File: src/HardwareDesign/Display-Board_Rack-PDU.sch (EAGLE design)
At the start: 46 parts

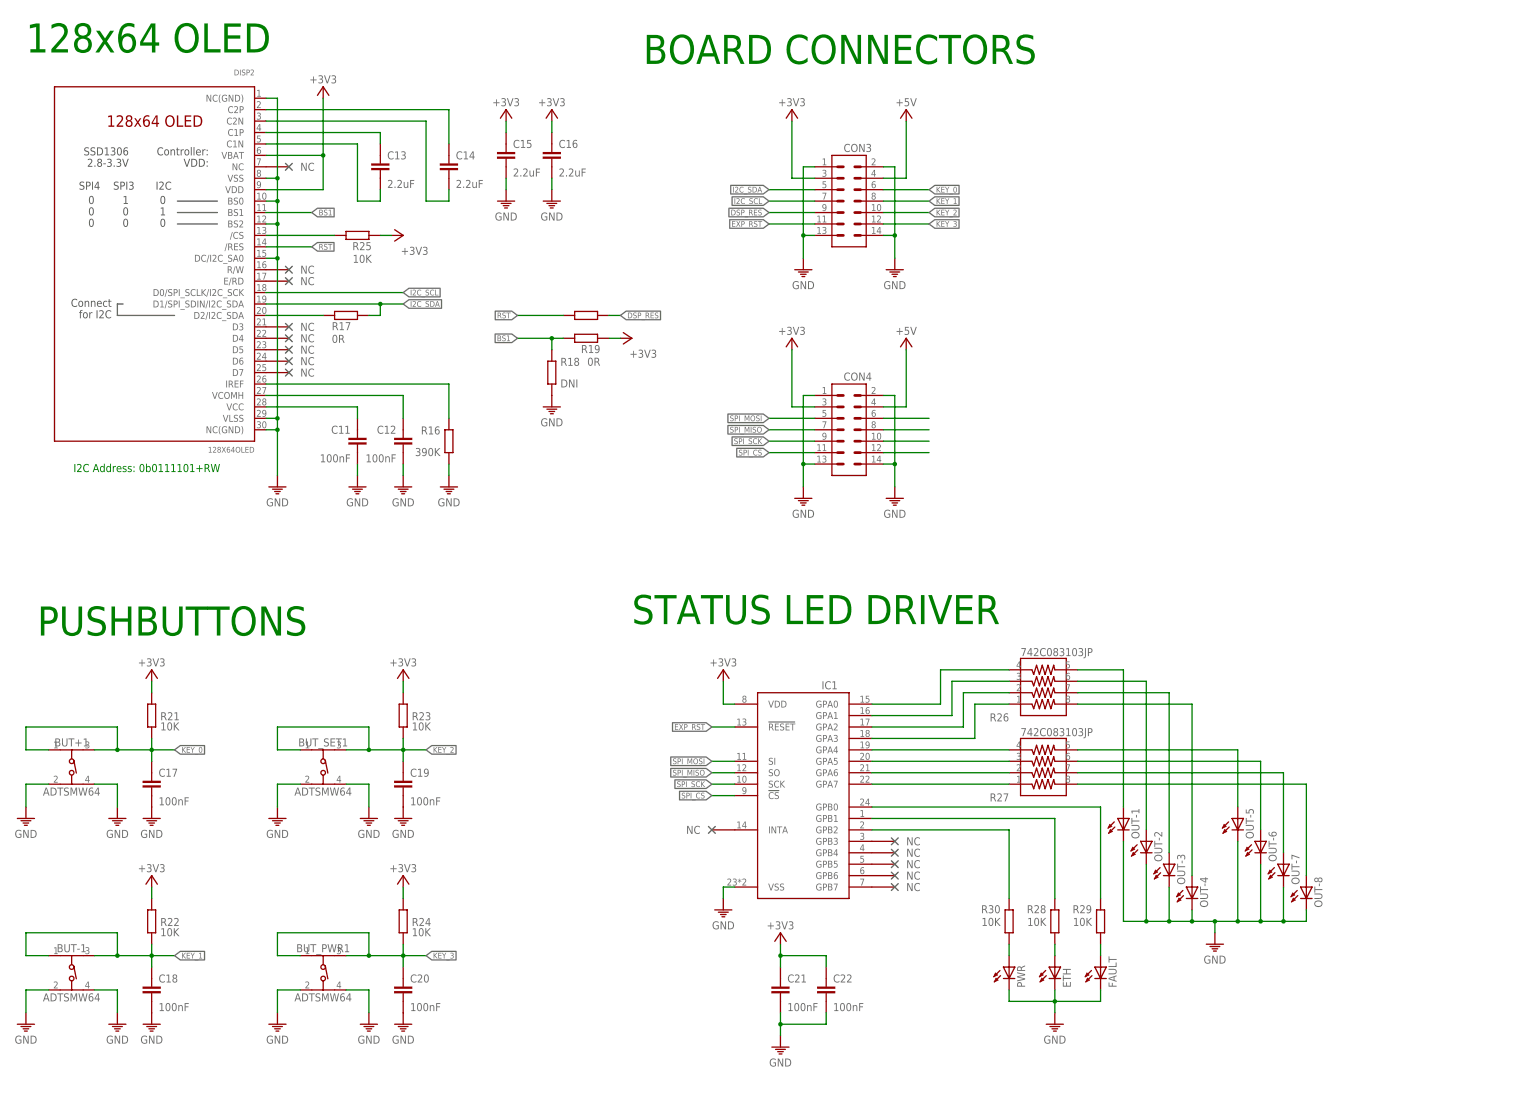
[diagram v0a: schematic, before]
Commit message: finish relay board design
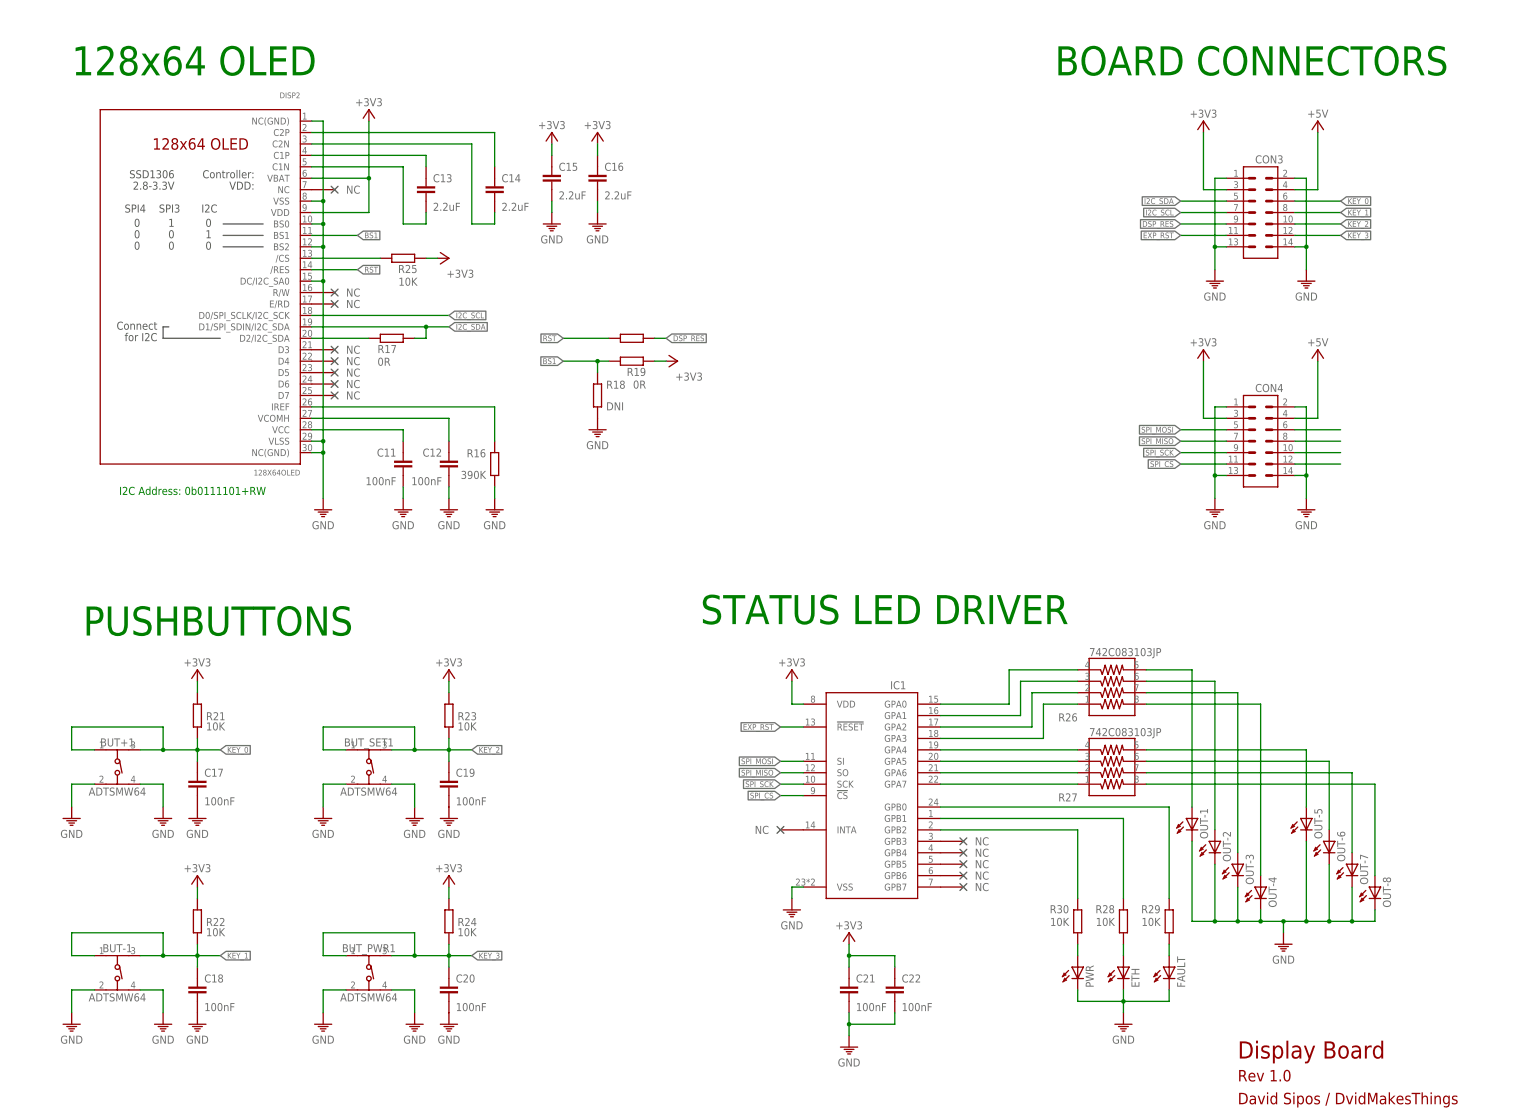
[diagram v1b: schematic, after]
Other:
- note added: "David Sipos / DvidMakesThings"
- note added: "Display Board"
- note added: "Rev 1.0"
- moved on the sheet: BUT+1, BUT-1, BUT_PWR1, BUT_SET1, C11, C12, C13, C14, C15, C16, C17, C18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

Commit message: first order send to JLCPCB
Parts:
- BUT+1, BUT-1, BUT_PWR1, BUT_SET1: value ADTSMW64 -> TC-6601-5.0-160
- ETH: value (none) -> XL-2012UBC
- FAULT: value (none) -> XL-2012SURC
- IC1: value (none) -> MCP23S18-E/MJ
- R26, R27: value 742C083103JP -> 4D03WGJ0102T5E 1K
- R28, R29, R30: value 10K -> 1K
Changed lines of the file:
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@@
 <part name="+3V17" library="ds_passive" deviceset="+3V3" device=""/>
 <part name="P+4" library="ds_passive" deviceset="+5V" device=""/>
-<part name="BUT+1" library="Wurth_Switch_WS-TASV" library_urn="urn:adsk.eagle:library:18304196" deviceset="430182043816" device="" package3d_urn="urn:adsk.eagle:package:18304300/2" value="ADTSMW64"/>
+<part name="BUT+1" library="Wurth_Switch_WS-TASV" library_urn="urn:adsk.eagle:library:18304196" deviceset="430182043816" device="" package3d_urn="urn:adsk.eagle:package:18304300/2" value="TC-6601-5.0-160"/>
 <part name="R21" library="ds_passive" deviceset="R" device="0402" package3d_urn="urn:adsk.eagle:package:46683744/2" value="10K"/>
 <part name="C17" library="ds_passive" deviceset="C" device="0402" package3d_urn="urn:adsk.eagle:package:46683744/2" value="100nF"/>
@@
 <part name="GND39" library="ds_passive" deviceset="GND" device=""/>
 <part name="+3V19" library="ds_passive" deviceset="+3V3" device=""/>
-<part name="BUT-1" library="Wurth_Switch_WS-TASV" library_urn="urn:adsk.eagle:library:18304196" deviceset="430182043816" device="" package3d_urn="urn:adsk.eagle:package:18304300/2" value="ADTSMW64"/>
+<part name="BUT-1" library="Wurth_Switch_WS-TASV" library_urn="urn:adsk.eagle:library:18304196" deviceset="430182043816" device="" package3d_urn="urn:adsk.eagle:package:18304300/2" value="TC-6601-5.0-160"/>
 <part name="R22" library="ds_passive" deviceset="R" device="0402" package3d_urn="urn:adsk.eagle:package:46683744/2" value="10K"/>
 <part name="C18" library="ds_passive" deviceset="C" device="0402" package3d_urn="urn:adsk.eagle:package:46683744/2" value="100nF"/>
@@
 <part name="GND42" library="ds_passive" deviceset="GND" device=""/>
 <part name="+3V20" library="ds_passive" deviceset="+3V3" device=""/>
-<part name="BUT_SET1" library="Wurth_Switch_WS-TASV" library_urn="urn:adsk.eagle:library:18304196" deviceset="430182043816" device="" package3d_urn="urn:adsk.eagle:package:18304300/2" value="ADTSMW64"/>
+<part name="BUT_SET1" library="Wurth_Switch_WS-TASV" library_urn="urn:adsk.eagle:library:18304196" deviceset="430182043816" device="" package3d_urn="urn:adsk.eagle:package:18304300/2" value="TC-6601-5.0-160"/>
 <part name="R23" library="ds_passive" deviceset="R" device="0402" package3d_urn="urn:adsk.eagle:package:46683744/2" value="10K"/>
 <part name="C19" library="ds_passive" deviceset="C" device="0402" package3d_urn="urn:adsk.eagle:package:46683744/2" value="100nF"/>
@@
 <part name="GND45" library="ds_passive" deviceset="GND" device=""/>
 <part name="+3V22" library="ds_passive" deviceset="+3V3" device=""/>
-<part name="BUT_PWR1" library="Wurth_Switch_WS-TASV" library_urn="urn:adsk.eagle:library:18304196" deviceset="430182043816" device="" package3d_urn="urn:adsk.eagle:package:18304300/2" value="ADTSMW64"/>
+<part name="BUT_PWR1" library="Wurth_Switch_WS-TASV" library_urn="urn:adsk.eagle:library:18304196" deviceset="430182043816" device="" package3d_urn="urn:adsk.eagle:package:18304300/2" value="TC-6601-5.0-160"/>
 <part name="R24" library="ds_passive" deviceset="R" device="0402" package3d_urn="urn:adsk.eagle:package:46683744/2" value="10K"/>
 <part name="C20" library="ds_passive" deviceset="C" device="0402" package3d_urn="urn:adsk.eagle:package:46683744/2" value="100nF"/>
@@
 <part name="GND49" library="ds_passive" deviceset="GND" device=""/>
 <part name="GND50" library="ds_passive" deviceset="GND" device=""/>
-<part name="IC1" library="ds_ic_peripherals" deviceset="MCP23S18" device="" package3d_urn="urn:adsk.eagle:package:46683902/2"/>
+<part name="IC1" library="ds_ic_peripherals" deviceset="MCP23S18" device="" package3d_urn="urn:adsk.eagle:package:46683902/2" value="MCP23S18-E/MJ"/>
 <part name="R25" library="ds_passive" deviceset="R" device="0402" package3d_urn="urn:adsk.eagle:package:46683744/2" value="10K"/>
 <part name="+3V26" library="ds_passive" deviceset="+3V3" device=""/>
@@
 <part name="GND51" library="ds_passive" deviceset="GND" device=""/>
 <part name="DISP2" library="ds_displays" deviceset="128X64OLED" device="" package3d_urn="urn:adsk.eagle:package:46762453/2"/>
-<part name="R26" library="Resistor Array" library_urn="urn:adsk.eagle:library:16491332" deviceset="742C083103JP" device="" package3d_urn="urn:adsk.eagle:package:16445849/4"/>
-<part name="R27" library="Resistor Array" library_urn="urn:adsk.eagle:library:16491332" deviceset="742C083103JP" device="" package3d_urn="urn:adsk.eagle:package:16445849/4"/>
-<part name="R28" library="ds_passive" deviceset="R" device="0402" package3d_urn="urn:adsk.eagle:package:46683744/2" value="10K"/>
-<part name="R29" library="ds_passive" deviceset="R" device="0402" package3d_urn="urn:adsk.eagle:package:46683744/2" value="10K"/>
-<part name="R30" library="ds_passive" deviceset="R" device="0402" package3d_urn="urn:adsk.eagle:package:46683744/2" value="10K"/>
-<part name="FAULT" library="led" library_urn="urn:adsk.eagle:library:259" deviceset="LED" device="CHIP-LED0805" package3d_urn="urn:adsk.eagle:package:15818/2"/>
-<part name="ETH" library="led" library_urn="urn:adsk.eagle:library:259" deviceset="LED" device="CHIP-LED0805" package3d_urn="urn:adsk.eagle:package:15818/2"/>
+<part name="R26" library="Resistor Array" library_urn="urn:adsk.eagle:library:16491332" deviceset="742C083103JP" device="" package3d_urn="urn:adsk.eagle:package:16445849/4" value="4D03WGJ0102T5E 1K"/>
+<part name="R27" library="Resistor Array" library_urn="urn:adsk.eagle:library:16491332" deviceset="742C083103JP" device="" package3d_urn="urn:adsk.eagle:package:16445849/4" value="4D03WGJ0102T5E 1K"/>
+<part name="R28" library="ds_passive" deviceset="R" device="0402" package3d_urn="urn:adsk.eagle:package:46683744/2" value="1K"/>
+<part name="R29" library="ds_passive" deviceset="R" device="0402" package3d_urn="urn:adsk.eagle:package:46683744/2" value="1K"/>
+<part name="R30" library="ds_passive" deviceset="R" device="0402" package3d_urn="urn:adsk.eagle:package:46683744/2" value="1K"/>
+<part name="FAULT" library="led" library_urn="urn:adsk.eagle:library:259" deviceset="LED" device="CHIP-LED0805" package3d_urn="urn:adsk.eagle:package:15818/2" value="XL-2012SURC"/>
+<part name="ETH" library="led" library_urn="urn:adsk.eagle:library:259" deviceset="LED" device="CHIP-LED0805" package3d_urn="urn:adsk.eagle:package:15818/2" value="XL-2012UBC"/>
 <part name="PWR" library="led" library_urn="urn:adsk.eagle:library:259" deviceset="LED" device="CHIP-LED0805" package3d_urn="urn:adsk.eagle:package:15818/2"/>
 <part name="GND52" library="ds_passive" deviceset="GND" device=""/>
